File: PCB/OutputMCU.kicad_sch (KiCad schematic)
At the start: 14 parts, among them J1 DAC_OUT, J2 SPI, J3 RST, J4 DAC, J5 SWD, U1 MSPM0G1507SPTR

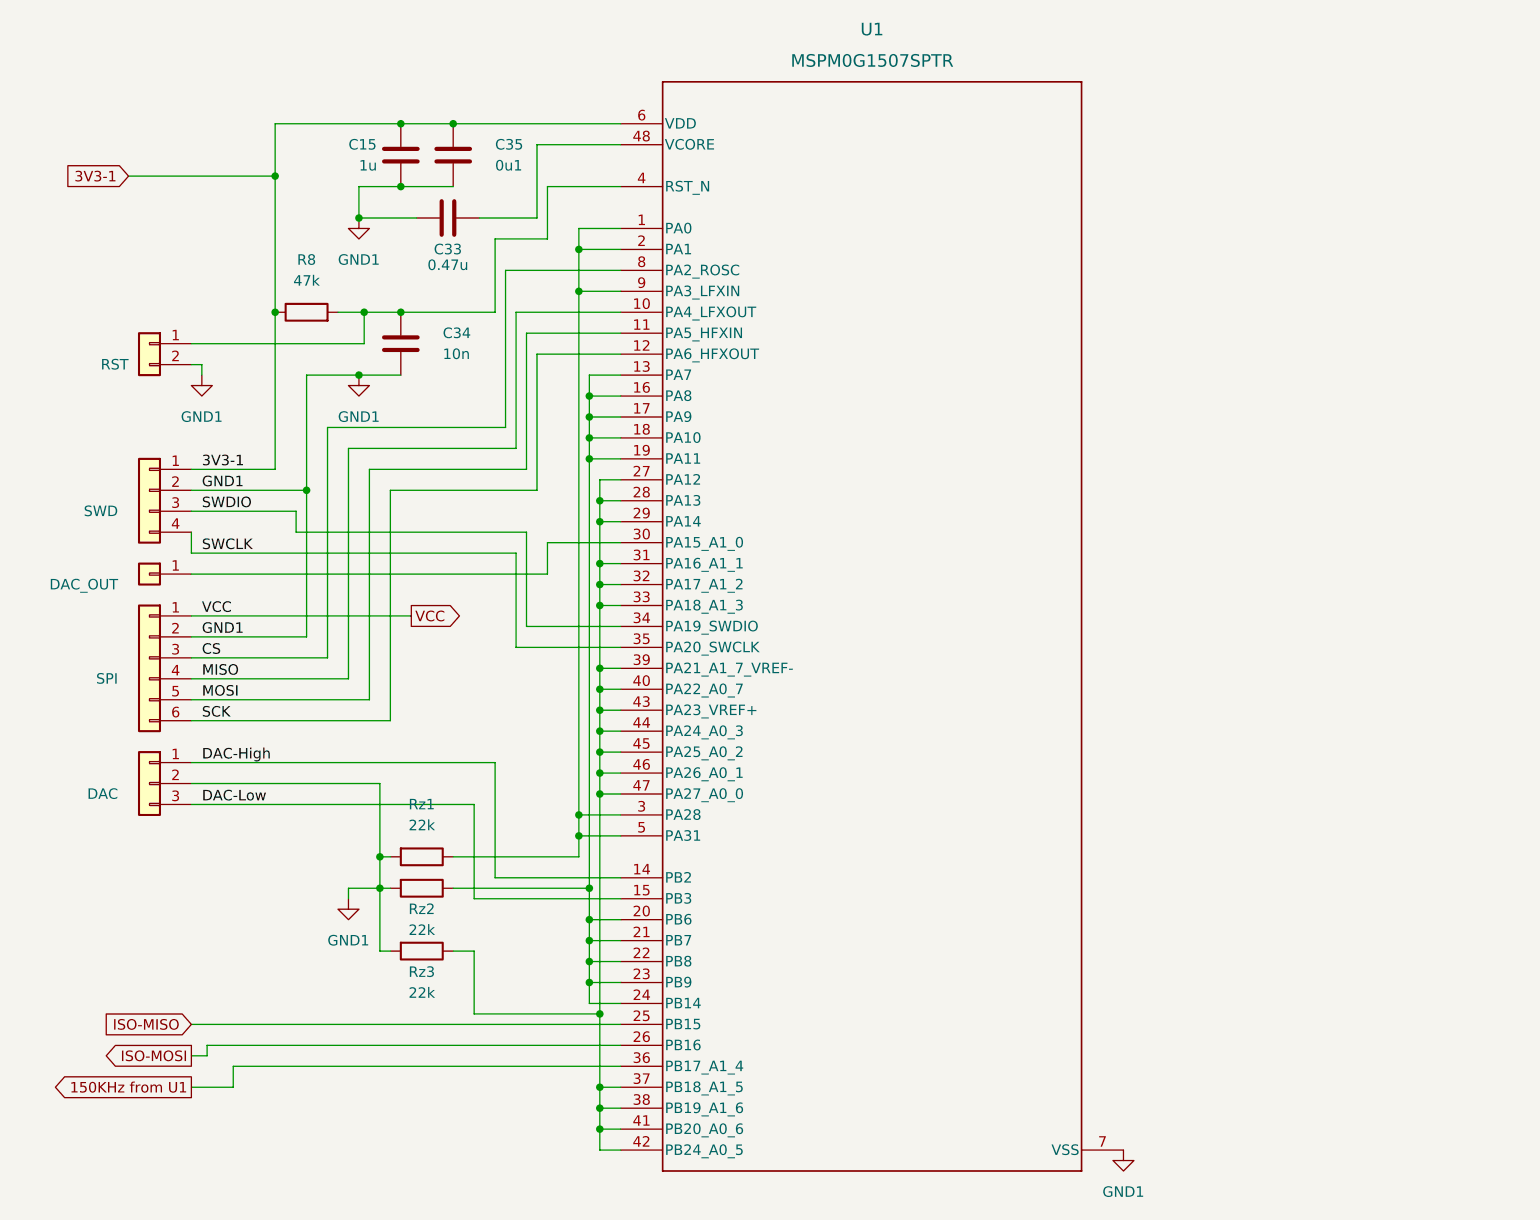
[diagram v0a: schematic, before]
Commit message: Remove files from obsolete RevA, in preparation for RevC progress.
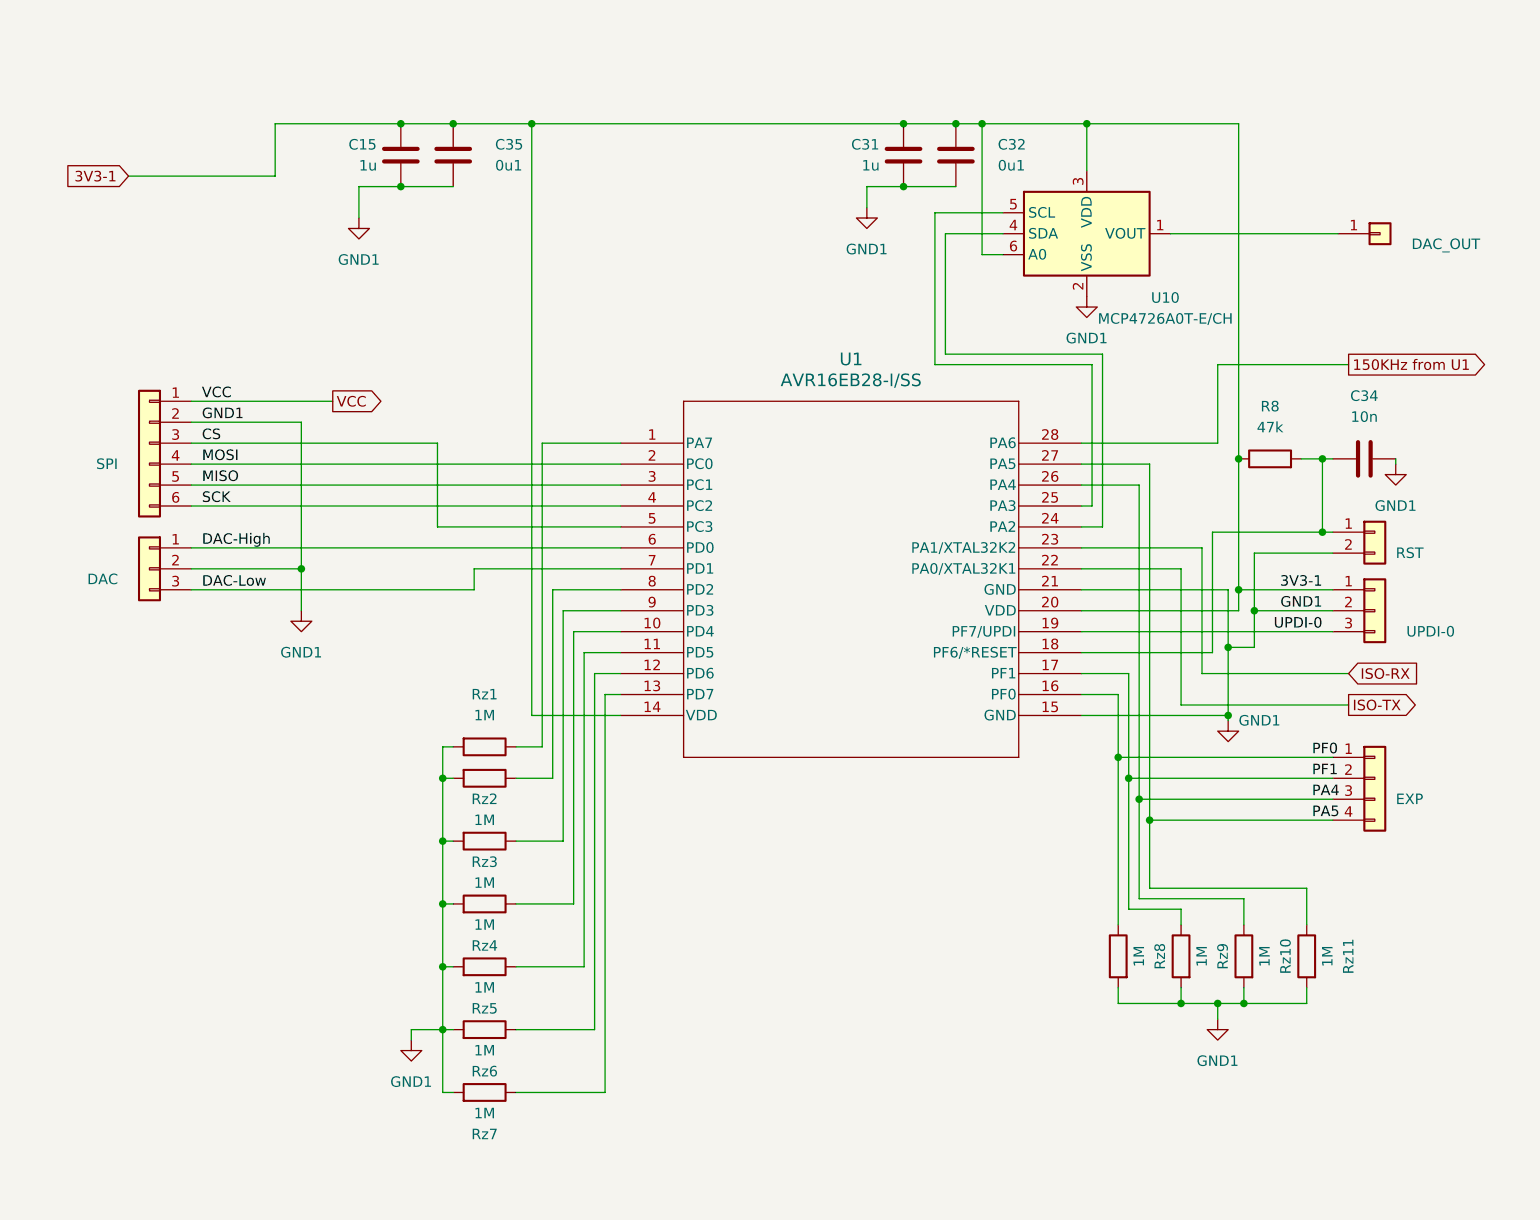
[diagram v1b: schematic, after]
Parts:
- removed C33: 0.47u, Capacitor_SMD:C_0402_1005Metric, symbol Device:C
- removed U1: MSPM0G1507SPTR, Package_QFP:LQFP-48_7x7mm_P0.5mm, symbol MSPM0G1507SPTR:MSPM0G1507SPTR
- added C31: 1u, Capacitor_SMD:C_0402_1005Metric, symbol Device:C
- added C32: 0u1, Capacitor_SMD:C_0402_1005Metric, symbol Device:C
- added J7: EXP, Connector_PinHeader_2.54mm:PinHeader_1x04_P2.54mm_Vertical, symbol Connector_Generic:Conn_01x04
- added Rz10, Rz11, Rz4, Rz5, Rz6, Rz7, Rz8, Rz9: 1M, Resistor_SMD:R_0603_1608Metric, symbol Device:R
- added U1: AVR16EB28-I/SS, Package_SO:SSOP28_SS_MCH, symbol MCU_Microchip_AVR:AVR16EB28-I_SS
- added U10: MCP4726A0T-E/CH, Package_TO_SOT_SMD:SOT-23-6, symbol Analog_DAC:MCP4725xxx-xCH
- J5: value SWD -> UPDI-0; footprint Connector_PinHeader_2.54mm:PinHeader_1x04_P2.54mm_Vertical -> Connector_PinHeader_2.54mm:PinHeader_1x03_P2.54mm_Vertical; symbol Connector_Generic:Conn_01x04 -> Connector_Generic:Conn_01x03
- Rz1, Rz2, Rz3: value 22k -> 1M
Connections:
- net 150KHz from U1: now also U1.28 (PA6)
- net 3V3-1: now also C31.1, C32.1, U1.14 (VDD), U1.20 (VDD), U10.3 (VDD), U10.6 (A0)
- net CS: now also U1.5 (PC3)
- net DAC-High: now also U1.6 (PD0)
- net DAC-Low: now also U1.7 (PD1)
- net GND1: now also C34.1, C31.2, C32.2, Rz10.2, Rz11.2, Rz4.2, Rz5.2, Rz6.2, Rz7.2, Rz8.2, Rz9.2, U1.15 (GND), U1.21 (GND), U10.2 (VSS); no longer C34.2
- net MISO: now also J2.5 (Pin_5), U1.3 (PC1); no longer J2.4 (Pin_4)
- net MOSI: now also J2.4 (Pin_4), U1.2 (PC0); no longer J2.5 (Pin_5)
- net SCK: now also U1.4 (PC2)
- net at Rz1.1: now also U1.1 (PA7)
- net at Rz2.1: now also U1.8 (PD2)
- net at Rz3.1: now also U1.9 (PD3)
- net at J1.1 (Pin_1): now also U10.1 (VOUT)
- net at J3.1 (Pin_1), R8.2: now also C34.2, U1.18 (PF6/*RESET); no longer C34.1
- removed net SWCLK: J5.4 (Pin_4)
- net SWDIO renamed UPDI-0
- net UPDI-0: now also U1.19 (PF7/UPDI)
- new net: Rz7.1, U1.13 (PD7)
- new net: U1.24 (PA2), U10.4 (SDA)
- new net: U1.25 (PA3), U10.5 (SCL)
- new net: Rz5.1, U1.11 (PD5)
- new net: Rz4.1, U1.10 (PD4)
- new net: Rz6.1, U1.12 (PD6)
- new net ISO-RX: U1.23 (PA1/XTAL32K2)
- new net ISO-TX: U1.22 (PA0/XTAL32K1)
- new net PA4: J7.3 (Pin_3), Rz10.1, U1.26 (PA4)
- new net PA5: J7.4 (Pin_4), Rz11.1, U1.27 (PA5)
- new net PF0: J7.1 (Pin_1), Rz8.1, U1.16 (PF0)
- new net PF1: J7.2 (Pin_2), Rz9.1, U1.17 (PF1)
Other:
- moved on the sheet: C34, R8, Rz1, Rz2, Rz3
